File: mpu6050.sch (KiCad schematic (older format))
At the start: 6 parts, among them U2 MPU6050

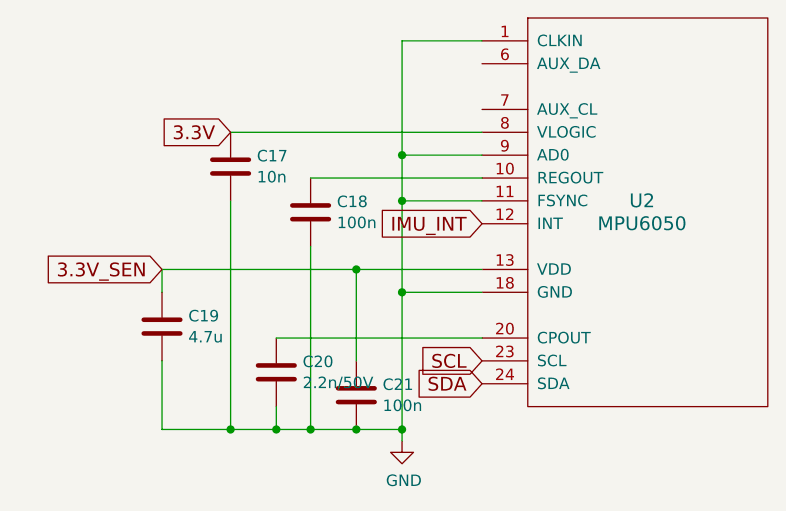
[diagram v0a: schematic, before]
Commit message: routing finished - essential signals only
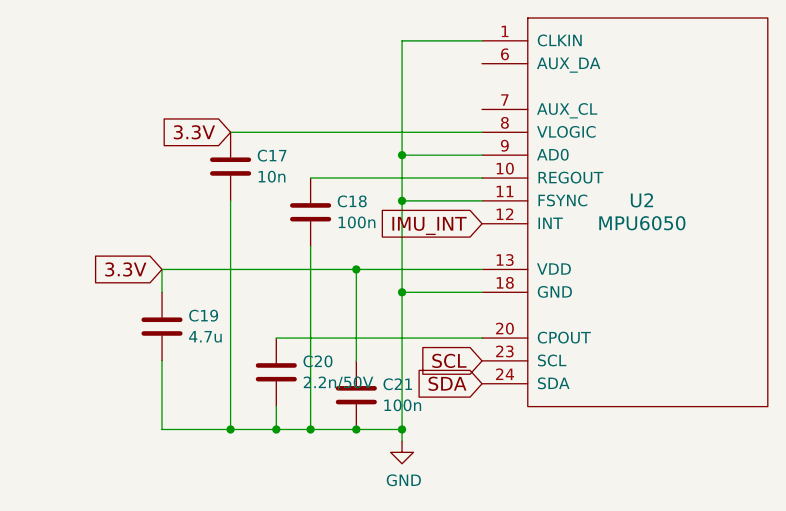
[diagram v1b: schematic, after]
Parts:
- C17, C18, C20, C21: footprint Capacitors_SMD:C_0603 -> Capacitors_SMD:C_0402
- C19: footprint Capacitors_SMD:C_0805 -> Capacitors_SMD:C_0603
- U2: footprint Housings_DFN_QFN:QFN-24-1EP_4x4mm_Pitch0.5mm -> alis_parts:QFN-24-noEP_4x4mm_Pitch0.5mm
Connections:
- net 3.3V_SEN is gone; now on net 3.3V: C19.1, C21.1, U2.13 (VDD)
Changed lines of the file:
@@
 $Descr A4 11693 8268
 encoding utf-8
-Sheet 4 8
+Sheet 4 7
 Title ""
 Date ""
@@
 F 0 "C18" H 5165 3546 50  0000 L CNN
 F 1 "100n" H 5165 3454 50  0000 L CNN
-F 2 "Capacitors_SMD:C_0603" H 5088 3350 50  0001 C CNN
+F 2 "Capacitors_SMD:C_0402" H 5088 3350 50  0001 C CNN
 F 3 "" H 5050 3500 50  0000 C CNN
 	1    5050 3500
@@
 F 0 "C17" H 4815 3346 50  0000 L CNN
 F 1 "10n" H 4815 3254 50  0000 L CNN
-F 2 "Capacitors_SMD:C_0603" H 4738 3150 50  0001 C CNN
+F 2 "Capacitors_SMD:C_0402" H 4738 3150 50  0001 C CNN
 F 3 "" H 4700 3300 50  0000 C CNN
 	1    4700 3300
@@
 F 0 "C21" H 5365 4346 50  0000 L CNN
 F 1 "100n" H 5365 4254 50  0000 L CNN
-F 2 "Capacitors_SMD:C_0603" H 5288 4150 50  0001 C CNN
+F 2 "Capacitors_SMD:C_0402" H 5288 4150 50  0001 C CNN
 F 3 "" H 5250 4300 50  0000 C CNN
 	1    5250 4300
@@
 F 0 "C20" H 5015 4246 50  0000 L CNN
 F 1 "2.2n/50V" H 5015 4154 50  0000 L CNN
-F 2 "Capacitors_SMD:C_0603" H 4938 4050 50  0001 C CNN
+F 2 "Capacitors_SMD:C_0402" H 4938 4050 50  0001 C CNN
 F 3 "" H 4900 4200 50  0000 C CNN
 	1    4900 4200
@@
 $EndComp
 $Comp
-L GND #PWR018
+L GND #PWR012
 U 1 1 569B8F29
 P 5450 4500
-F 0 "#PWR018" H 5450 4250 50  0001 C CNN
+F 0 "#PWR012" H 5450 4250 50  0001 C CNN
 F 1 "GND" H 5458 4326 50  0000 C CNN
 F 2 "" H 5450 4500 50  0000 C CNN
@@
 F 0 "U2" H 6500 3550 60  0000 C CNN
 F 1 "MPU6050" H 6500 3450 60  0000 C CNN
-F 2 "Housings_DFN_QFN:QFN-24-1EP_4x4mm_Pitch0.5mm" H 6450 3300 60  0001 C CNN
+F 2 "alis_parts:QFN-24-noEP_4x4mm_Pitch0.5mm" H 6450 3300 60  0001 C CNN
 F 3 "" H 6450 3300 60  0000 C CNN
 	1    6500 3500
@@
 F 0 "C19" H 4515 4046 50  0000 L CNN
 F 1 "4.7u" H 4515 3954 50  0000 L CNN
-F 2 "Capacitors_SMD:C_0805" H 4438 3850 50  0001 C CNN
+F 2 "Capacitors_SMD:C_0603" H 4438 3850 50  0001 C CNN
 F 3 "" H 4400 4000 50  0000 C CNN
 	1    4400 4000
@@
 	4400 3750 4400 3850
 Text GLabel 4400 3750 0    60   Input ~ 0
-3.3V_SEN
+3.3V
 Wire Wire Line
 	5250 4150 5250 3750
